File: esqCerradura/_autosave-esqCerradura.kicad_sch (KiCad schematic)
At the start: 19 parts, among them J1 Screw_Terminal_01x02, Q1 BC337, U1 PC817, U2 L7805, U3 arduino_relay

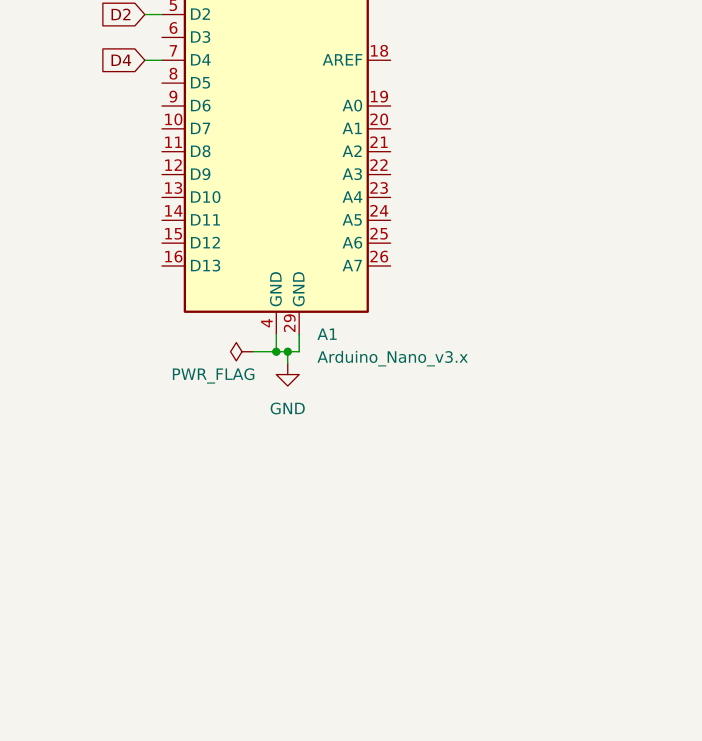
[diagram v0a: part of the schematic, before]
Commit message: Se agrega esquemático en PNG
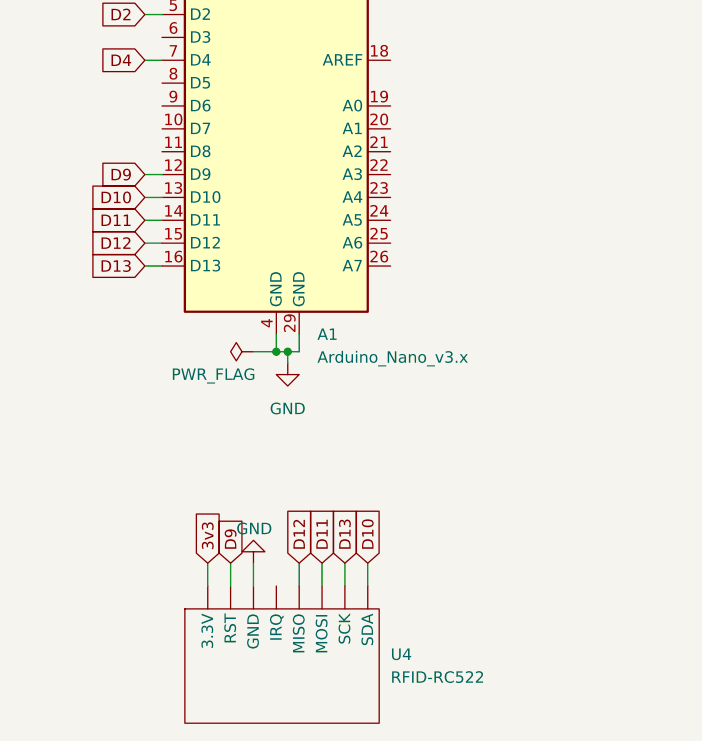
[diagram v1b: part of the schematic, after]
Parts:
- added U4: RFID-RC522, symbol arduino:RFID-RC522
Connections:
- net 3v3: now also U4. (SDA)
- net GND: now also U4. (SDA)
- net D9: now reaches A1.12 (D9)
- net D9: now also U4. (SDA)
- net D10: now reaches A1.13 (D10)
- net D10: now also U4. (SDA)
- net D11: now reaches A1.14 (D11)
- net D11: now also U4. (SDA)
- net D12: now reaches A1.15 (D12)
- net D12: now also U4. (SDA)
- net D13: now reaches A1.16 (D13)
- net D13: now also U4. (SDA)
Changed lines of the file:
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@@
   (junction (at 49.53 118.11) (diameter 0) (color 0 0 0 0)
   )
+  (wire (pts (xy 46.99 141.605) (xy 46.99 144.145))
+    (stroke (width 0) (type default) (color 0 0 0 0))
+  )
   (wire (pts (xy 140.97 80.645) (xy 139.065 80.645))
     (stroke (width 0) (type default) (color 0 0 0 0))
@@
     (stroke (width 0) (type default) (color 0 0 0 0))
   )
+  (wire (pts (xy 34.925 108.585) (xy 36.83 108.585))
+    (stroke (width 0) (type default) (color 0 0 0 0))
+  )
   (wire (pts (xy 198.755 78.105) (xy 206.375 78.105))
     (stroke (width 0) (type default) (color 0 0 0 0))
@@
     (stroke (width 0) (type default) (color 0 0 0 0))
   )
+  (wire (pts (xy 41.91 141.605) (xy 41.91 144.145))
+    (stroke (width 0) (type default) (color 0 0 0 0))
+  )
   (wire (pts (xy 37.465 27.94) (xy 37.465 26.67))
     (stroke (width 0) (type default) (color 0 0 0 0))
@@
     (stroke (width 0) (type default) (color 0 0 0 0))
   )
+  (wire (pts (xy 59.69 141.605) (xy 59.69 144.145))
+    (stroke (width 0) (type default) (color 0 0 0 0))
+  )
   (wire (pts (xy 49.53 116.205) (xy 49.53 118.11))
     (stroke (width 0) (type default) (color 0 0 0 0))
@@
     (stroke (width 0) (type default) (color 0 0 0 0))
   )
+  (wire (pts (xy 34.925 106.045) (xy 36.83 106.045))
+    (stroke (width 0) (type default) (color 0 0 0 0))
+  )
   (wire (pts (xy 177.165 31.115) (xy 177.165 32.385))
     (stroke (width 0) (type default) (color 0 0 0 0))
@@
     (stroke (width 0) (type default) (color 0 0 0 0))
   )
+  (wire (pts (xy 52.07 141.605) (xy 52.07 144.145))
+    (stroke (width 0) (type default) (color 0 0 0 0))
+  )
+  (wire (pts (xy 57.15 141.605) (xy 57.15 144.145))
+    (stroke (width 0) (type default) (color 0 0 0 0))
+  )
   (wire (pts (xy 69.85 37.465) (xy 65.405 37.465))
     (stroke (width 0) (type default) (color 0 0 0 0))
   )
+  (wire (pts (xy 34.925 98.425) (xy 36.83 98.425))
+    (stroke (width 0) (type default) (color 0 0 0 0))
+  )
   (wire (pts (xy 159.385 121.285) (xy 158.75 121.285))
     (stroke (width 0) (type default) (color 0 0 0 0))
@@
     (stroke (width 0) (type default) (color 0 0 0 0))
   )
+  (wire (pts (xy 34.925 100.965) (xy 36.83 100.965))
+    (stroke (width 0) (type default) (color 0 0 0 0))
+  )
   (wire (pts (xy 145.415 40.005) (xy 145.415 42.545))
     (stroke (width 0) (type default) (color 0 0 0 0))
@@
     (stroke (width 0) (type default) (color 0 0 0 0))
   )
+  (wire (pts (xy 54.61 141.605) (xy 54.61 144.145))
+    (stroke (width 0) (type default) (color 0 0 0 0))
+  )
   (wire (pts (xy 158.75 104.14) (xy 158.75 106.045))
     (stroke (width 0) (type default) (color 0 0 0 0))
@@
   (wire (pts (xy 135.89 70.485) (xy 139.065 70.485))
     (stroke (width 0) (type default) (color 0 0 0 0))
+  )
+  (wire (pts (xy 44.45 141.605) (xy 44.45 144.145))
+    (stroke (width 0) (type default) (color 0 0 0 0))
+  )
+  (wire (pts (xy 34.925 103.505) (xy 36.83 103.505))
+    (stroke (width 0) (type default) (color 0 0 0 0))
+  )
+  (global_label "D12" (shape input) (at 34.925 106.045 180) (fields_autoplaced)
+    (effects (font (size 1.27 1.27)) (justify right))
+    (property "Intersheet References" "${INTERSHEET_REFS}" (id 0) (at 28.8229 106.1244 0)
+      (effects (font (size 1.27 1.27)) (justify right) hide)
+    )
   )
   (global_label "D2" (shape input) (at 34.925 80.645 180) (fields_autoplaced)
@@
     )
   )
+  (global_label "D13" (shape input) (at 57.15 141.605 90) (fields_autoplaced)
+    (effects (font (size 1.27 1.27)) (justify left))
+    (property "Intersheet References" "${INTERSHEET_REFS}" (id 0) (at 57.0706 135.5029 90)
+      (effects (font (size 1.27 1.27)) (justify left) hide)
+    )
+  )
   (global_label "3v3" (shape input) (at 52.07 62.865 90) (fields_autoplaced)
     (effects (font (size 1.27 1.27)) (justify left))
     (property "Intersheet References" "${INTERSHEET_REFS}" (id 0) (at 51.9906 57.0652 90)
+      (effects (font (size 1.27 1.27)) (justify left) hide)
+    )
+  )
+  (global_label "3v3" (shape input) (at 41.91 141.605 90) (fields_autoplaced)
+    (effects (font (size 1.27 1.27)) (justify left))
+    (property "Intersheet References" "${INTERSHEET_REFS}" (id 0) (at 41.8306 135.8052 90)
       (effects (font (size 1.27 1.27)) (justify left) hide)
     )
@@
     )
   )
+  (global_label "D11" (shape input) (at 54.61 141.605 90) (fields_autoplaced)
+    (effects (font (size 1.27 1.27)) (justify left))
+    (property "Intersheet References" "${INTERSHEET_REFS}" (id 0) (at 54.5306 135.5029 90)
+      (effects (font (size 1.27 1.27)) (justify left) hide)
+    )
+  )
+  (global_label "D10" (shape input) (at 59.69 141.605 90) (fields_autoplaced)
+    (effects (font (size 1.27 1.27)) (justify left))
+    (property "Intersheet References" "${INTERSHEET_REFS}" (id 0) (at 59.6106 135.5029 90)
+      (effects (font (size 1.27 1.27)) (justify left) hide)
+    )
+  )
   (global_label "5v" (shape input) (at 42.545 23.495 90) (fields_autoplaced)
     (effects (font (size 1.27 1.27)) (justify left))
@@
     )
   )
+  (global_label "D9" (shape input) (at 34.925 98.425 180) (fields_autoplaced)
+    (effects (font (size 1.27 1.27)) (justify right))
+    (property "Intersheet References" "${INTERSHEET_REFS}" (id 0) (at 30.0324 98.3456 0)
+      (effects (font (size 1.27 1.27)) (justify right) hide)
+    )
+  )
+  (global_label "D9" (shape input) (at 44.45 141.605 90) (fields_autoplaced)
+    (effects (font (size 1.27 1.27)) (justify left))
+    (property "Intersheet References" "${INTERSHEET_REFS}" (id 0) (at 44.5294 136.7124 90)
+      (effects (font (size 1.27 1.27)) (justify left) hide)
+    )
+  )
   (global_label "12v" (shape input) (at 201.93 74.295 0) (fields_autoplaced)
     (effects (font (size 1.27 1.27)) (justify left))
@@
     )
   )
+  (global_label "D13" (shape input) (at 34.925 108.585 180) (fields_autoplaced)
+    (effects (font (size 1.27 1.27)) (justify right))
+    (property "Intersheet References" "${INTERSHEET_REFS}" (id 0) (at 28.8229 108.6644 0)
+      (effects (font (size 1.27 1.27)) (justify right) hide)
+    )
+  )
   (global_label "3v3" (shape input) (at 65.405 24.13 90) (fields_autoplaced)
     (effects (font (size 1.27 1.27)) (justify left))
     (property "Intersheet References" "${INTERSHEET_REFS}" (id 0) (at 65.3256 18.3302 90)
       (effects (font (size 1.27 1.27)) (justify left) hide)
+    )
+  )
+  (global_label "D10" (shape input) (at 34.925 100.965 180) (fields_autoplaced)
+    (effects (font (size 1.27 1.27)) (justify right))
+    (property "Intersheet References" "${INTERSHEET_REFS}" (id 0) (at 28.8229 101.0444 0)
+      (effects (font (size 1.27 1.27)) (justify right) hide)
+    )
+  )
+  (global_label "D11" (shape input) (at 34.925 103.505 180) (fields_autoplaced)
+    (effects (font (size 1.27 1.27)) (justify right))
+    (property "Intersheet References" "${INTERSHEET_REFS}" (id 0) (at 28.8229 103.5844 0)
+      (effects (font (size 1.27 1.27)) (justify right) hide)
     )
   )
@@
     )
   )
+  (global_label "D12" (shape input) (at 52.07 141.605 90) (fields_autoplaced)
+    (effects (font (size 1.27 1.27)) (justify left))
+    (property "Intersheet References" "${INTERSHEET_REFS}" (id 0) (at 51.9906 135.5029 90)
+      (effects (font (size 1.27 1.27)) (justify left) hide)
+    )
+  )
   (global_label "12v" (shape input) (at 151.765 29.845 90) (fields_autoplaced)
     (effects (font (size 1.27 1.27)) (justify left))
@@
     (pin "2")
   )
+  (symbol (lib_id "arduino:RFID-RC522") (at 39.37 146.685 270) (unit 1)
+    (in_bom yes) (on_board yes) (fields_autoplaced)
+    (property "Reference" "U4" (id 0) (at 62.23 151.7649 90)
+      (effects (font (size 1.27 1.27)) (justify left))
+    )
+    (property "Value" "RFID-RC522" (id 1) (at 62.23 154.3049 90)
+      (effects (font (size 1.27 1.27)) (justify left))
+    )
+    (property "Footprint" "" (id 2) (at 39.37 146.685 0)
+      (effects (font (size 1.27 1.27)) hide)
+    )
+    (property "Datasheet" "" (id 3) (at 39.37 146.685 0)
+      (effects (font (size 1.27 1.27)) hide)
+    )
+    (pin "")
+    (pin "")
+    (pin "")
+    (pin "")
+    (pin "")
+    (pin "")
+    (pin "")
+    (pin "")
+  )
   (symbol (lib_id "power:PWR_FLAG") (at 144.145 29.21 0) (unit 1)
     (in_bom yes) (on_board yes) (fields_autoplaced)
@@
     (pin "1")
     (pin "2")
+  )
+  (symbol (lib_id "power:GND") (at 46.99 141.605 180) (unit 1)
+    (in_bom yes) (on_board yes)
+    (property "Reference" "#PWR011" (id 0) (at 46.99 135.255 0)
+      (effects (font (size 1.27 1.27)) hide)
+    )
+    (property "Value" "GND" (id 1) (at 45.085 137.795 0)
+      (effects (font (size 1.27 1.27)) (justify right))
+    )
+    (property "Footprint" "" (id 2) (at 46.99 141.605 0)
+      (effects (font (size 1.27 1.27)) hide)
+    )
+    (property "Datasheet" "" (id 3) (at 46.99 141.605 0)
+      (effects (font (size 1.27 1.27)) hide)
+    )
+    (pin "1")
   )
   (symbol (lib_id "power:GND") (at 158.75 137.795 0) (unit 1)
@@
       (reference "#PWR010") (unit 1) (value "GND1") (footprint "")
     )
+    (path "/4398aa2b-3a8f-4514-b374-d6707d14029f"
+      (reference "#PWR011") (unit 1) (value "GND") (footprint "")
+    )
     (path "/e9ba2ba4-5ced-401b-be22-24c3cecc23e1"
       (reference "A1") (unit 1) (value "Arduino_Nano_v3.x") (footprint "Module:Arduino_Nano")
@@
       (reference "U3") (unit 1) (value "arduino_relay") (footprint "")
     )
-  )
+    (path "/2219d9d5-c12e-41fe-8e4e-2d25d97914e4"
+      (reference "U4") (unit 1) (value "RFID-RC522") (footprint "")
+    )
+  )
